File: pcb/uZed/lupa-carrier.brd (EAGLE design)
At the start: 101.6 x 57.1 mm, 104 parts, among them J5 HDMI-TYPE-A-RECEPTICALFCI1002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, J6 HDMI-TYPE-A-RECEPTICALFCI1002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, K1 694108105102

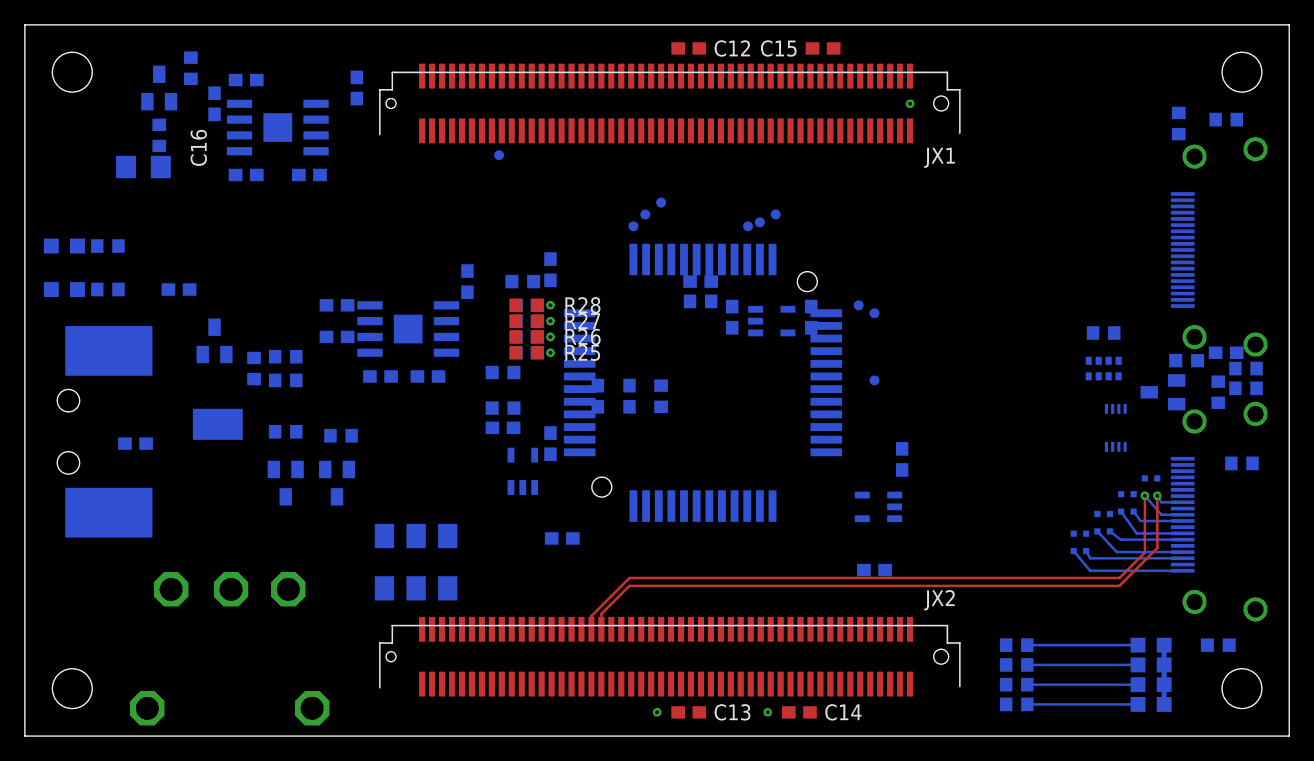
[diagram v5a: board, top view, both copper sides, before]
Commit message: routed hdmi and lupa data lines
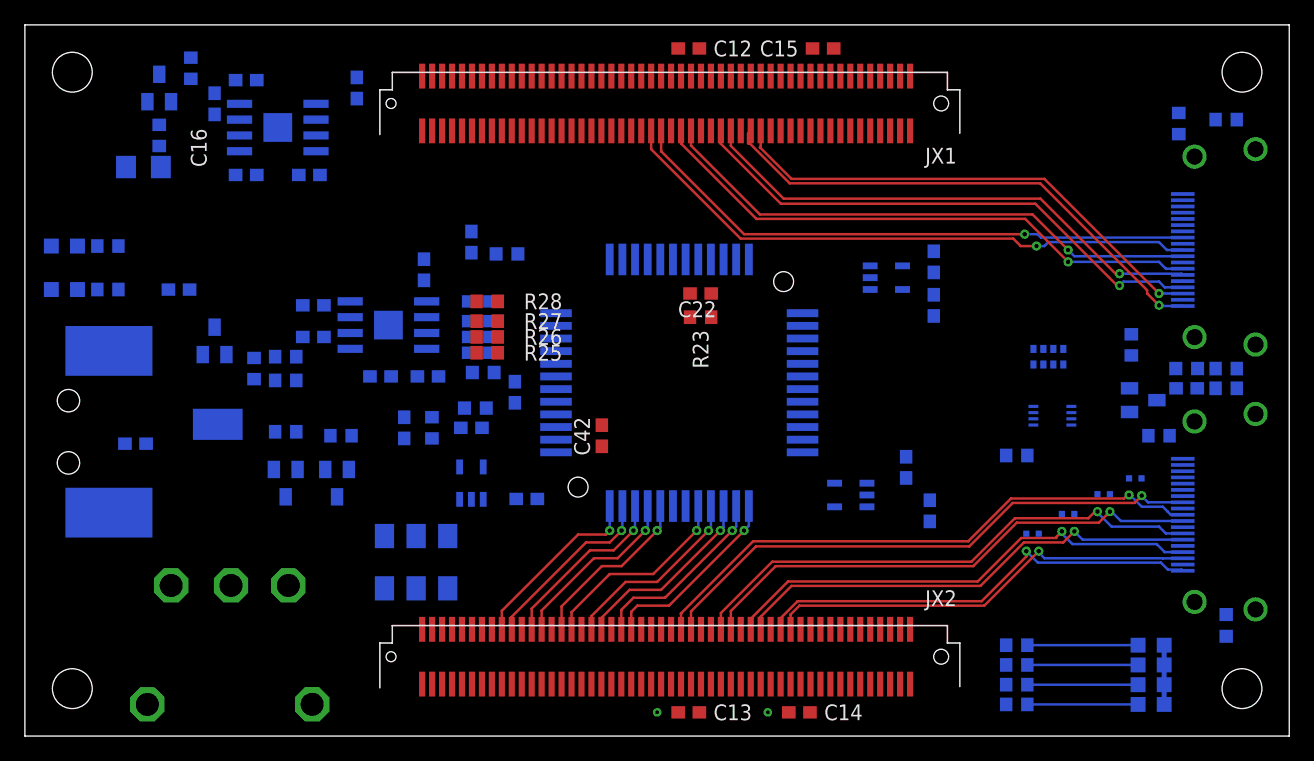
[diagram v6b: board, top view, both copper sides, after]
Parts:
- removed FR_VAL, INT1, INT2, INT3, LN_VAL, POW_EN, RESET, SPI_CLK, SPI_DATA, SPI_EN: TPTP08R, testpad:TP08R
- moved R24 18.6 mm to (32.7, 24.8)
- moved C23 18.3 mm to (30.5, 24.8)
- moved C38 16.8 mm to (73.0, 38.1)
- moved R22 12.1 mm to (79.7, 22.5)
- moved C37 9.89 mm to (73.0, 34.6)
- moved U$6 9.85 mm to (69.2, 36.8)
- moved R31 7.96 mm to (88.9, 31.4), turned to 270 degrees
- moved R30 7.03 mm to (91.1, 24.1), turned to 0 degrees
- moved C20 6.73 mm to (35.9, 39.7)
- moved C5 6.68 mm to (39.4, 27.6)
- moved C39 6.51 mm to (72.7, 18.1), turned to 270 degrees
- moved PCA9306 5.17 mm to (82.5, 25.7), turned to 90 degrees
- moved RN7 4.55 mm to (82.2, 30.5)
- moved C41 4.27 mm to (40.3, 19.1), turned to 180 degrees
- moved C32 4.27 mm to (93.3, 27.9)
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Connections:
- net CLK: now also JX1.P$59; no longer JX1.P$53
- net D0: now also JX2.P$58; no longer JX2.P$12
- net D1: now also JX2.P$60; no longer JX2.P$14
- net D2: now also JX2.P$64; no longer JX2.P$18
- net D3: now also JX2.P$66; no longer JX2.P$20
- net D4: now also JX2.P$70; no longer JX2.P$26
- net D5: now also JX2.P$72; no longer JX2.P$28
- net D6: now also JX2.P$76; no longer JX2.P$32
- net D7: now also JX2.P$78; no longer JX2.P$34
- net D8: now also JX2.P$82; no longer JX2.P$38
- net D9: now also JX2.P$84; no longer JX2.P$40
- net FRAME_VALID: now also JX1.P$34; no longer FR_VAL.TP, JX1.P$37
- net INT_TIME1: now also JX1.P$26; no longer INT1.TP, JX1.P$27
- net INT_TIME2: now also JX1.P$28; no longer INT2.TP, JX1.P$31
- net INT_TIME3: now also JX1.P$32; no longer INT3.TP, JX1.P$33
- net LINE_VALID: now also JX1.P$38; no longer JX1.P$39, LN_VAL.TP
- net LPOWEN: no longer POW_EN.TP
- net P1_CLOCK+: now also JX2.P$48; no longer JX1.P$66, JX2.P$66
- net P1_CLOCK-: now also JX2.P$46; no longer JX1.P$64, JX2.P$64
- net P1_DATA0+: now also JX2.P$40; no longer JX1.P$72, JX2.P$72
- net P1_DATA0-: now also JX2.P$38; no longer JX1.P$70, JX2.P$70
- net P1_DATA1+: now also JX2.P$34; no longer JX1.P$78, JX2.P$78
- net P1_DATA1-: now also JX2.P$32; no longer JX1.P$76, JX2.P$76
- net P1_DATA2+: now also JX2.P$28; no longer JX1.P$84, JX2.P$84
- net P1_DATA2-: now also JX2.P$26; no longer JX1.P$82, JX2.P$82
- net P2_CLOCK+: now also JX1.P$53; no longer JX1.P$34
- net P2_CLOCK-: now also JX1.P$51; no longer JX1.P$32
- net P2_DATA0+: now also JX1.P$47; no longer JX1.P$40
- net P2_DATA0-: now also JX1.P$45; no longer JX1.P$38
- net P2_DATA1+: now also JX1.P$39; no longer JX1.P$48
- net P2_DATA1-: now also JX1.P$37; no longer JX1.P$46
- net P2_DATA2+: now also JX1.P$33; no longer JX1.P$54
- net P2_DATA2-: now also JX1.P$31; no longer JX1.P$52
- net RESET: now also JX1.P$40; no longer JX1.P$47, RESET.TP
- net SPI_CLK: no longer SPI_CLK.TP
- net SPI_DATA: no longer SPI_DATA.TP
- net SPI_EN: no longer SPI_EN.TP
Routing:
- net P2_CLOCK+: track 0.00 -> 47.8 mm, vias 0 -> 1
- net P2_CLOCK-: track 0.00 -> 46.4 mm, vias 0 -> 1
- net P2_DATA0+: track 0.00 -> 45.5 mm, vias 0 -> 1
- net P2_DATA0-: track 0.00 -> 44.4 mm, vias 0 -> 1
- net P2_DATA1+: track 0.00 -> 43.2 mm, vias 0 -> 1
- net P2_DATA1-: track 0.00 -> 41.8 mm, vias 0 -> 1
- net P2_DATA2+: track 0.00 -> 41.6 mm, vias 0 -> 1
- net P2_DATA2-: track 0.00 -> 40.2 mm, vias 0 -> 1
- net P1_DATA0-: track 4.32 -> 41.4 mm, vias 0 -> 1
- net P1_DATA0+: track 5.85 -> 42.6 mm, vias 0 -> 1
- net P1_DATA1+: track 7.57 -> 39.6 mm, vias 0 -> 1
- net P1_DATA1-: track 6.08 -> 38.0 mm, vias 0 -> 1
- net P1_DATA2-: track 8.09 -> 35.1 mm, vias 0 -> 1
- net P1_DATA2+: track 9.49 -> 36.3 mm, vias 0 -> 1
- net D4: track 0.00 -> 16.2 mm, vias 0 -> 1
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
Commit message: more layout
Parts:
- moved C3 20.5 mm to (22.2, 39.1)
- moved C23 16.9 mm to (46.4, 30.5), flipped to the top, turned to 180 degrees
- moved R24 14.2 mm to (46.4, 28.6), flipped to the top, turned to 0 degrees
- moved C7 10.7 mm to (21.6, 35.2)
- moved C4 10.6 mm to (46.4, 26.7), flipped to the top
- moved C31 10.6 mm to (33.3, 37.8), turned to 90 degrees
- moved C38 10.6 mm to (65.1, 31.1), turned to 270 degrees
- moved C30 10.2 mm to (33.3, 31.8), turned to 270 degrees
- moved U$2 9.26 mm to (18.7, 40.3)
- moved C42 6.99 mm to (39.4, 23.8), flipped to the bottom, turned to 0 degrees
- moved C1 6.73 mm to (11.7, 39.4)
- moved C20 6.73 mm to (42.2, 37.5), turned to 0 degrees
- moved C40 5.85 mm to (65.1, 22.9)
- moved U$6 5.79 mm to (68.3, 31.1), turned to 270 degrees
- moved C39 4.86 mm to (71.8, 22.9)
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
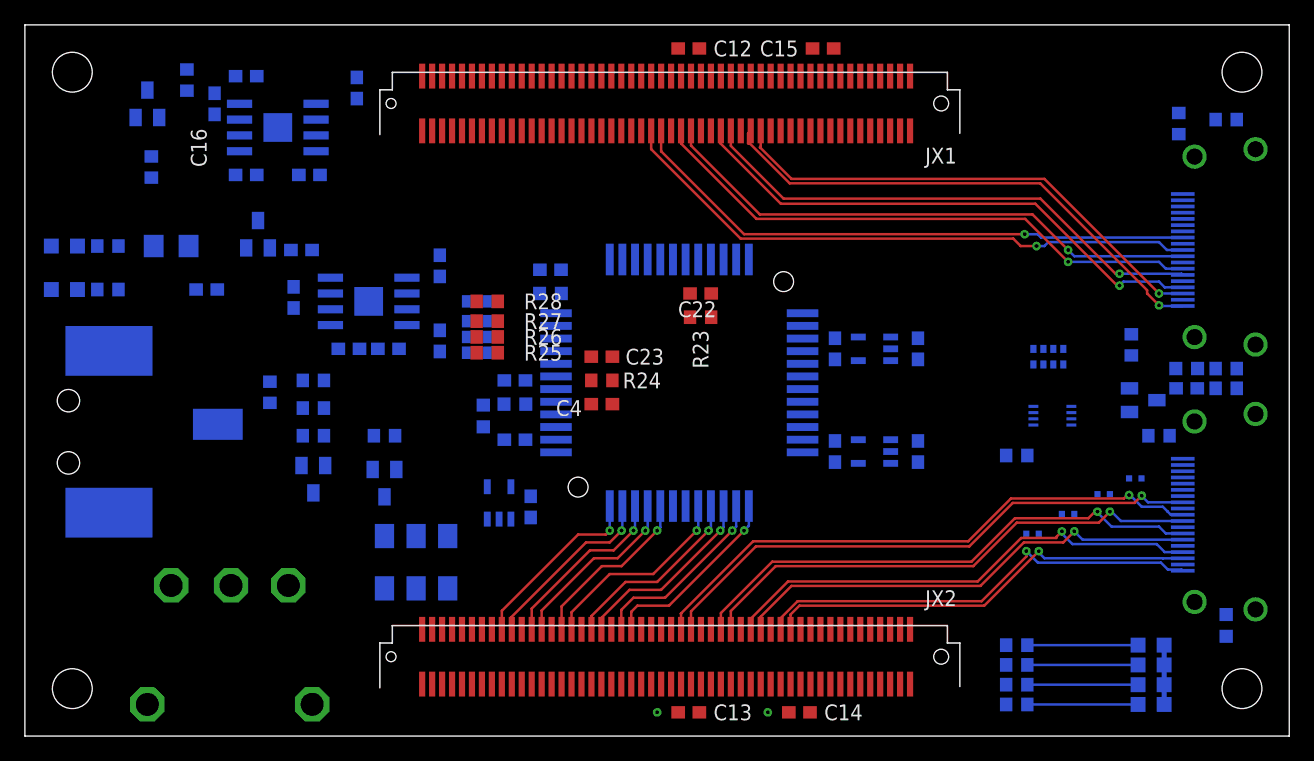
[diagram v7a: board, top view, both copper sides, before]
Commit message: lupa control signals routed
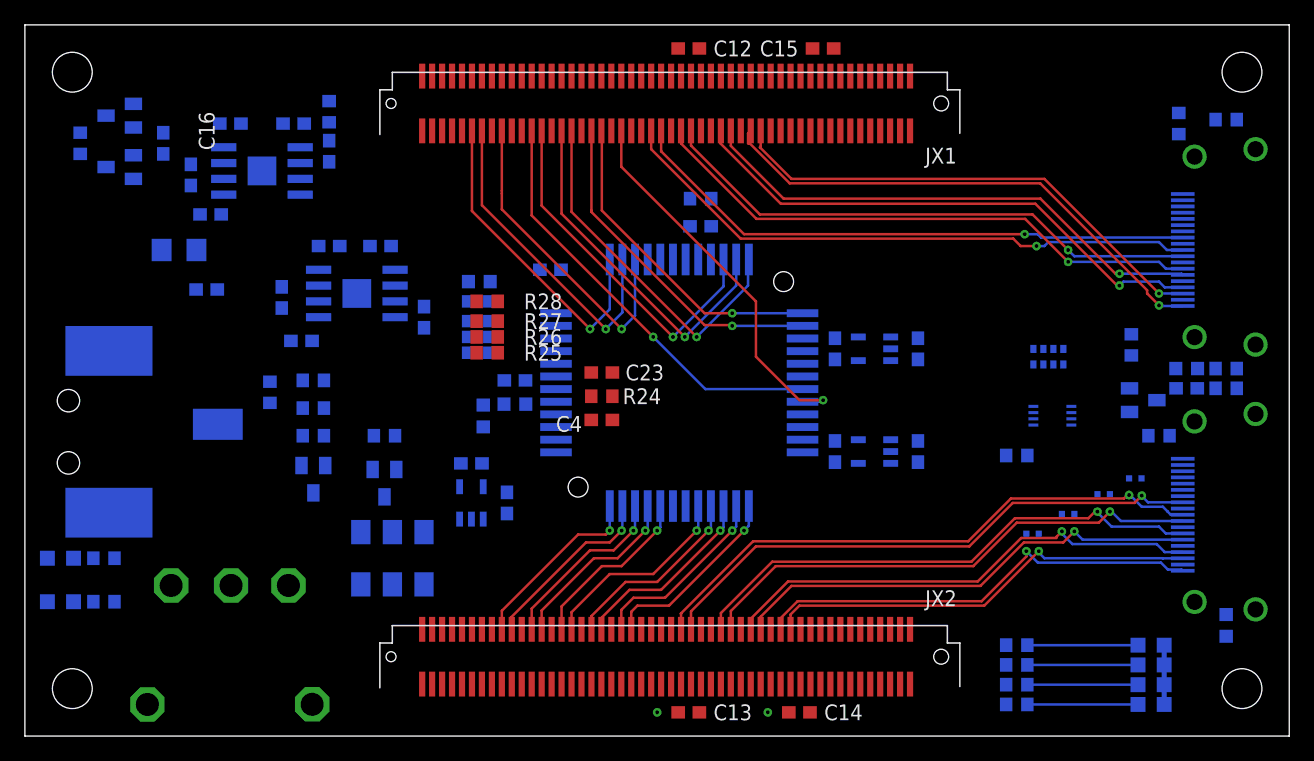
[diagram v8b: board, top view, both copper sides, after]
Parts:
- moved OFF 25.1 mm to (2.86, 14.3)
- moved ON 25.1 mm to (2.86, 10.8)
- moved R11 25.1 mm to (6.35, 10.8)
- moved R12 25.1 mm to (6.35, 14.3)
- moved C3 14.0 mm to (11.1, 47.6), turned to 90 degrees
- moved C30 13.2 mm to (20.6, 35.2)
- moved C31 12.6 mm to (22.2, 31.8), turned to 0 degrees
- moved U$2 12.4 mm to (7.62, 45.7), turned to 270 degrees
- moved R3 11.7 mm to (24.4, 50.2)
- moved C17 11.5 mm to (14.9, 41.9)
- moved C7 10.6 mm to (32.1, 33.7), turned to 270 degrees
- moved R23 9.52 mm to (54.3, 43.2), flipped to the bottom
- moved C29 8.41 mm to (24.4, 39.4), turned to 180 degrees
- moved C6 8.28 mm to (28.6, 39.4), turned to 0 degrees
- moved C19 7.57 mm to (16.5, 49.2), turned to 0 degrees
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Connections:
- net FRAME_VALID: now also JX1.P$71; no longer JX1.P$34
- net INT_TIME1: now also JX1.P$65; no longer JX1.P$26
- net INT_TIME2: now also JX1.P$63; no longer JX1.P$28
- net INT_TIME3: now also JX1.P$69; no longer JX1.P$32
- net LINE_VALID: now also JX1.P$75; no longer JX1.P$38
- net LPOWEN: now also JX1.P$90; no longer JX1.P$81
- net RESET: now also JX1.P$77; no longer JX1.P$40
- net SPI_CLK: now also JX1.P$87; no longer JX1.P$71
- net SPI_DATA: now also JX1.P$83; no longer JX1.P$69
- net SPI_EN: now also JX1.P$89; no longer JX1.P$75
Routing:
- net RESET: track 0.00 -> 34.3 mm, vias 0 -> 1
- net CLK: track 0.00 -> 31.2 mm, vias 0 -> 1
- net LINE_VALID: track 0.00 -> 28.8 mm, vias 0 -> 1
- net INT_TIME3: track 0.00 -> 28.7 mm, vias 0 -> 1
- net FRAME_VALID: track 0.00 -> 28.6 mm, vias 0 -> 1
- net INT_TIME1: track 0.00 -> 27.3 mm, vias 0 -> 1
- net SPI_CLK: track 0.00 -> 26.2 mm, vias 0 -> 1
- net SPI_EN: track 0.00 -> 26.1 mm, vias 0 -> 1
- net INT_TIME2: track 0.00 -> 26.0 mm, vias 0 -> 1
- net SPI_DATA: track 0.00 -> 25.9 mm, vias 0 -> 1
